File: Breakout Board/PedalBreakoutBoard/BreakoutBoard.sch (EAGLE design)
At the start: 15 parts, among them U1 ES_DAISY_SEED_REV4

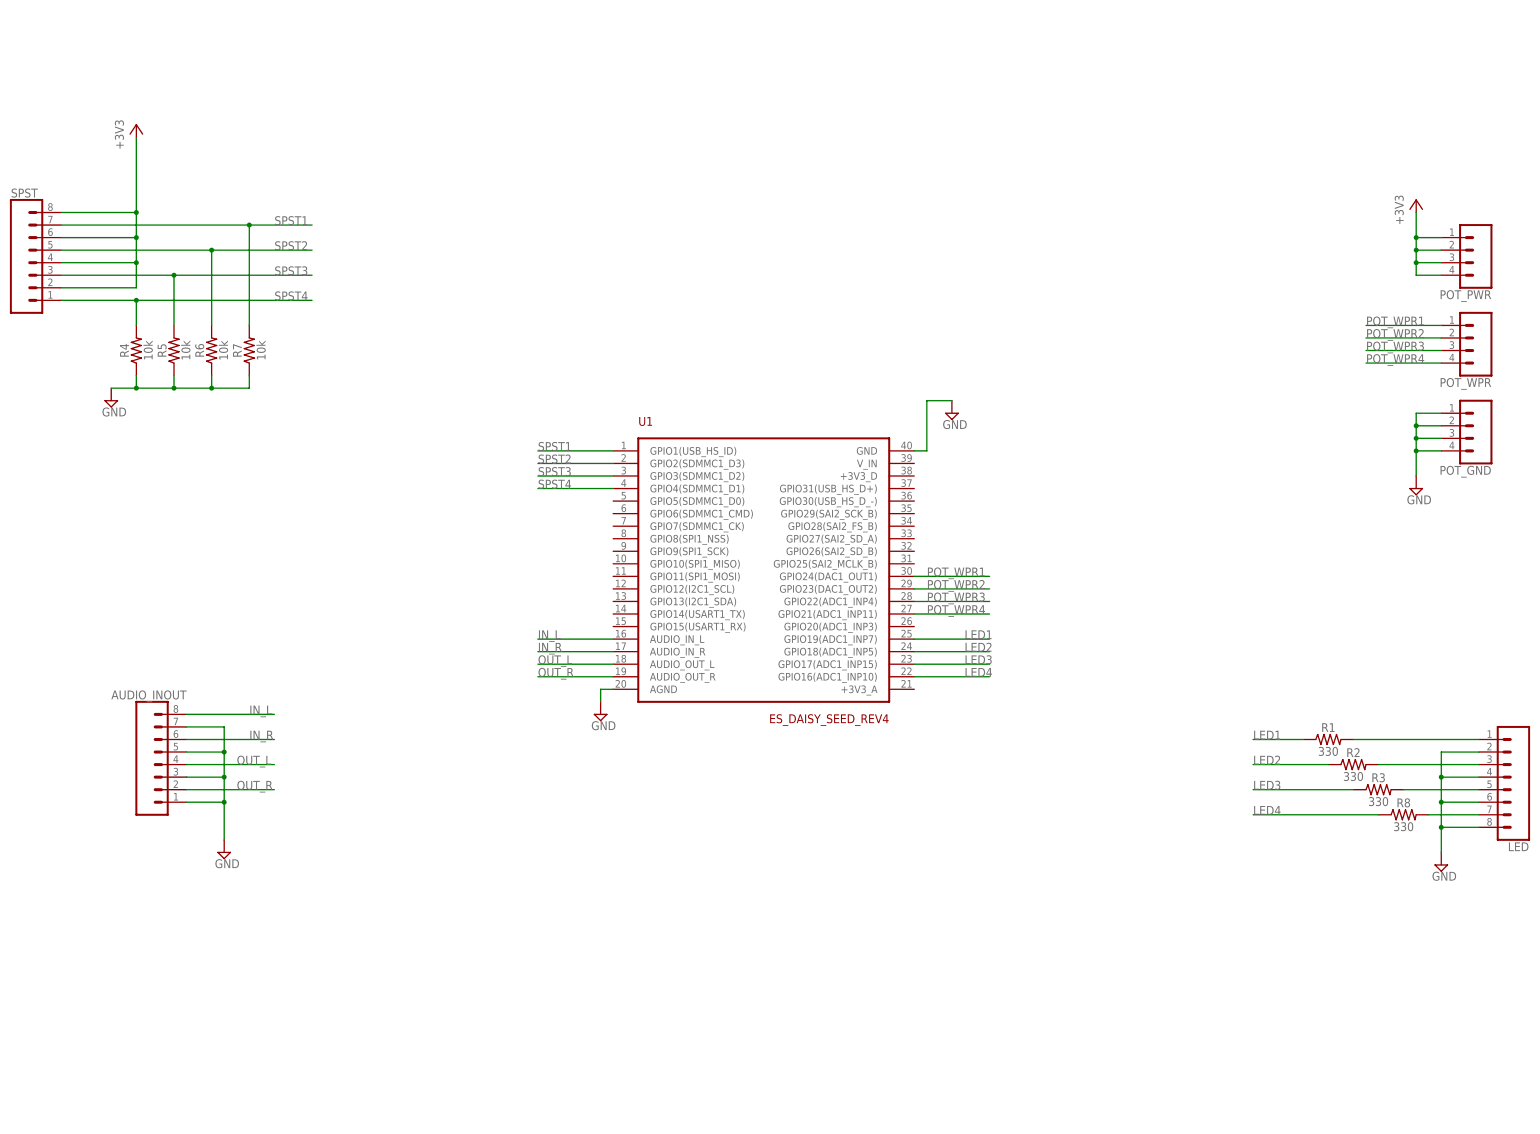
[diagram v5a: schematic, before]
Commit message: DP-16 - Add SPDT section
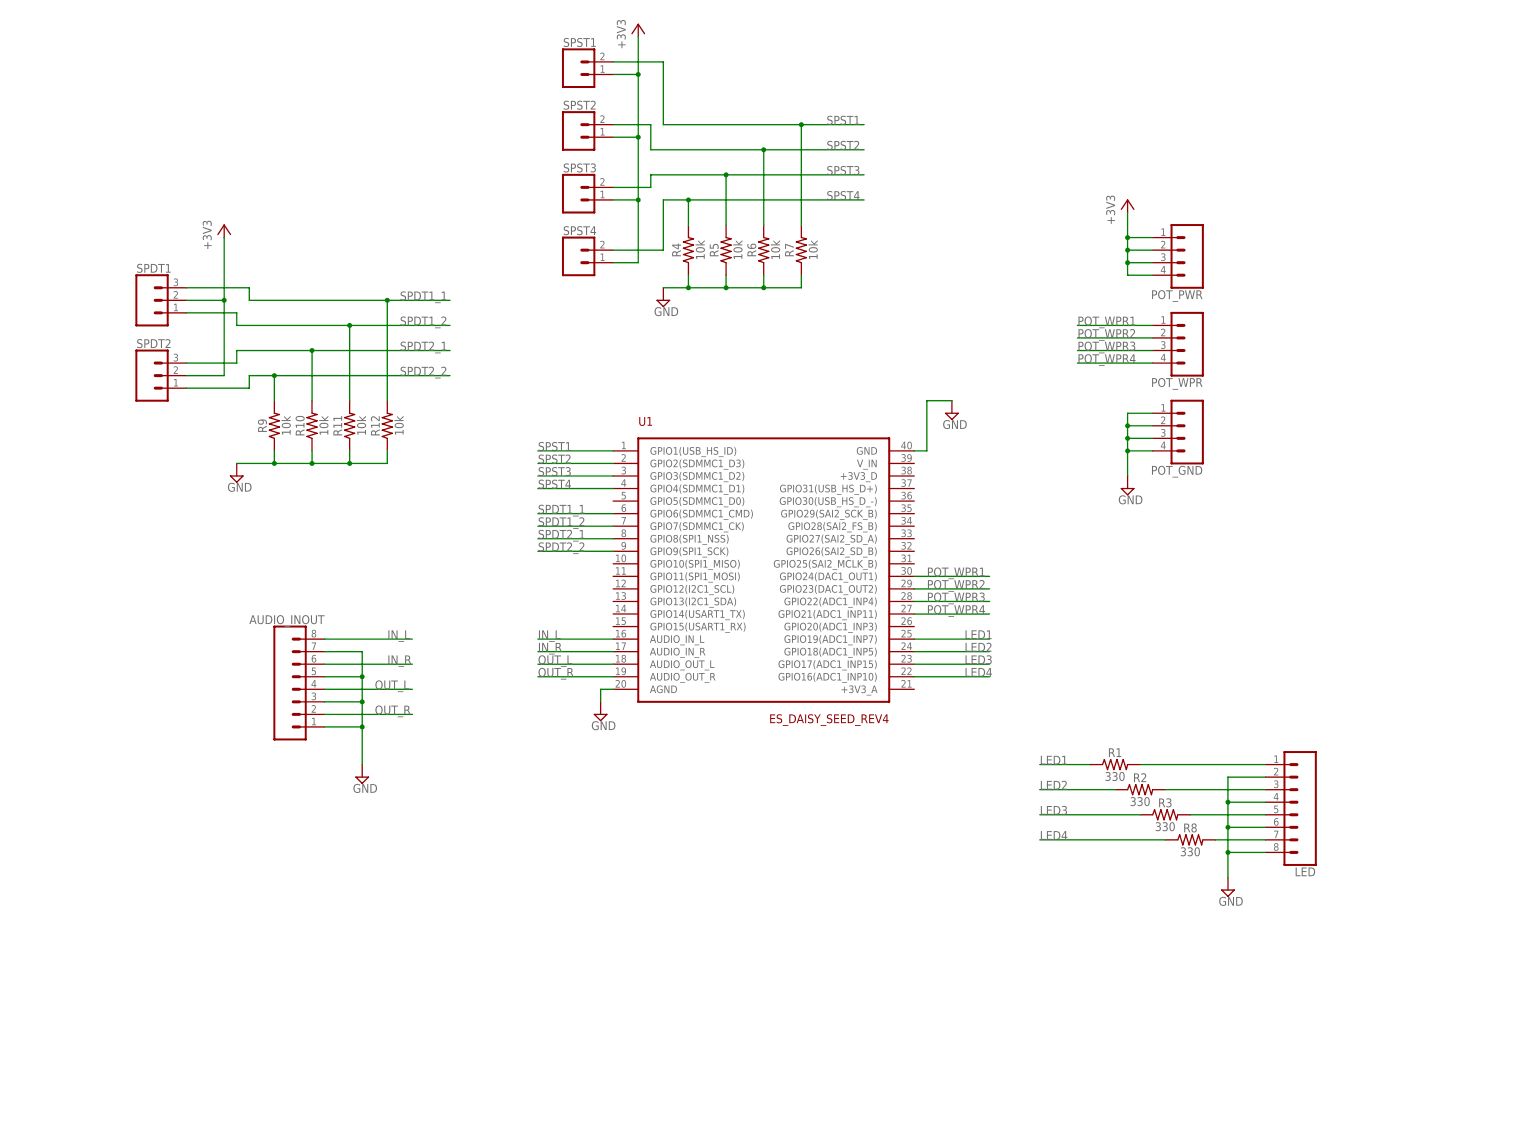
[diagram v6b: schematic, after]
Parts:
- removed SPST: (no value), SparkFun-Connectors:CONN_08"
- added R10, R11, R12, R9: 10k, SparkFun-Resistors:10KOHM-HORIZ-1/4W-5%
- added SPDT1, SPDT2: (no value), SparkFun-Connectors:CONN_03
- added SPST1, SPST2, SPST3, SPST4: (no value), SparkFun-Connectors:CONN_02
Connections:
- new net SPDT1_1: R12.2, SPDT1.3, U1.GPIO6(SDMMC1_CMD)
- new net SPDT1_2: R11.2, SPDT1.1, U1.GPIO7(SDMMC1_CK)
- new net SPDT2_1: R10.2, SPDT2.3, U1.GPIO8(SPI1_NSS)
- new net SPDT2_2: R9.2, SPDT2.1, U1.GPIO9(SPI1_SCK)
- net +3V3: now also SPDT1.2, SPDT2.2, SPST1.1, SPST2.1, SPST3.1, SPST4.1; no longer SPST.2, SPST.4, SPST.6, SPST.8
- net GND: now also R10.1, R11.1, R12.1, R9.1
- net SPST1: now also SPST1.2; no longer SPST.7
- net SPST2: now also SPST2.2; no longer SPST.5
- net SPST3: now also SPST3.2; no longer SPST.3
- net SPST4: now also SPST4.2; no longer SPST.1
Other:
- moved on the sheet: AUDIO_INOUT, LED, POT_GND, POT_PWR, POT_WPR, R1, R2, R3, R4, R5, R6, R7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

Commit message: DP-16 - Reorder groups for consistency
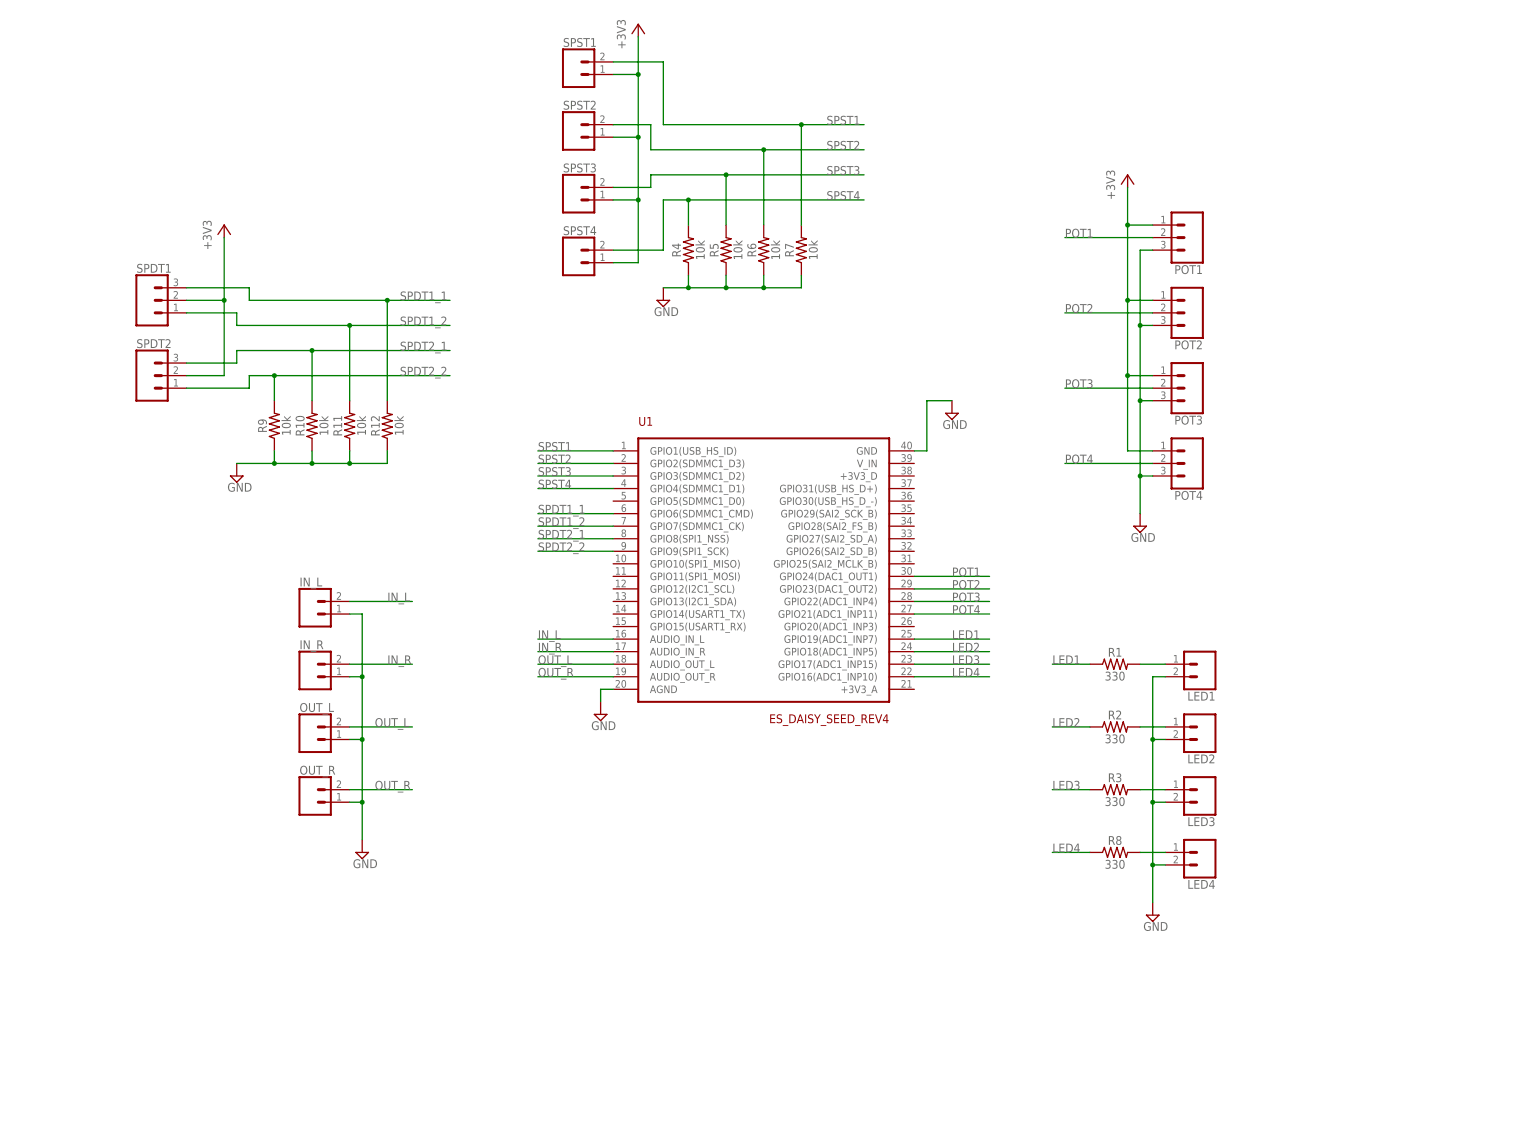
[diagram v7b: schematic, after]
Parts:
- removed AUDIO_INOUT, LED: (no value), SparkFun-Connectors:CONN_08"
- removed POT_GND, POT_PWR, POT_WPR: (no value), SparkFun-Connectors:CONN_04
- added IN_L, IN_R, LED1, LED2, LED3, LED4, OUT_L, OUT_R: (no value), SparkFun-Connectors:CONN_02
- added POT1, POT2, POT3, POT4: (no value), SparkFun-Connectors:CONN_03
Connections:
- removed net POT_WPR1: POT_WPR.1, U1.GPIO24(DAC1_OUT1)
- removed net POT_WPR2: POT_WPR.2, U1.GPIO23(DAC1_OUT2)
- removed net POT_WPR3: POT_WPR.3, U1.GPIO22(ADC1_INP4)
- removed net POT_WPR4: POT_WPR.4, U1.GPIO21(ADC1_INP11)
- new net POT1: POT1.2, U1.GPIO24(DAC1_OUT1)
- new net POT2: POT2.2, U1.GPIO23(DAC1_OUT2)
- new net POT3: POT3.2, U1.GPIO22(ADC1_INP4)
- new net POT4: POT4.2, U1.GPIO21(ADC1_INP11)
- net +3V3: now also POT1.1, POT2.1, POT3.1, POT4.1; no longer POT_PWR.1, POT_PWR.2, POT_PWR.3, POT_PWR.4
- net GND: now also IN_L.1, IN_R.1, LED1.2, LED2.2, LED3.2, LED4.2, OUT_L.1, OUT_R.1, POT1.3, POT2.3, POT3.3, POT4.3; no longer AUDIO_INOUT.1, AUDIO_INOUT.3, AUDIO_INOUT.5, AUDIO_INOUT.7, LED.2, LED.4, LED.6, LED.8, POT_GND.1, POT_GND.2, POT_GND.3, POT_GND.4
- net IN_L: now also IN_L.2; no longer AUDIO_INOUT.8
- net IN_R: now also IN_R.2; no longer AUDIO_INOUT.6
- net N$5: now also LED1.1; no longer LED.1
- net N$6: now also LED2.1; no longer LED.3
- net N$7: now also LED3.1; no longer LED.5
- net N$8: now also LED4.1; no longer LED.7
- net OUT_L: now also OUT_L.2; no longer AUDIO_INOUT.4
- net OUT_R: now also OUT_R.2; no longer AUDIO_INOUT.2
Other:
- moved on the sheet: R1, R2, R3, R8

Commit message: DP-16 - Add selector section
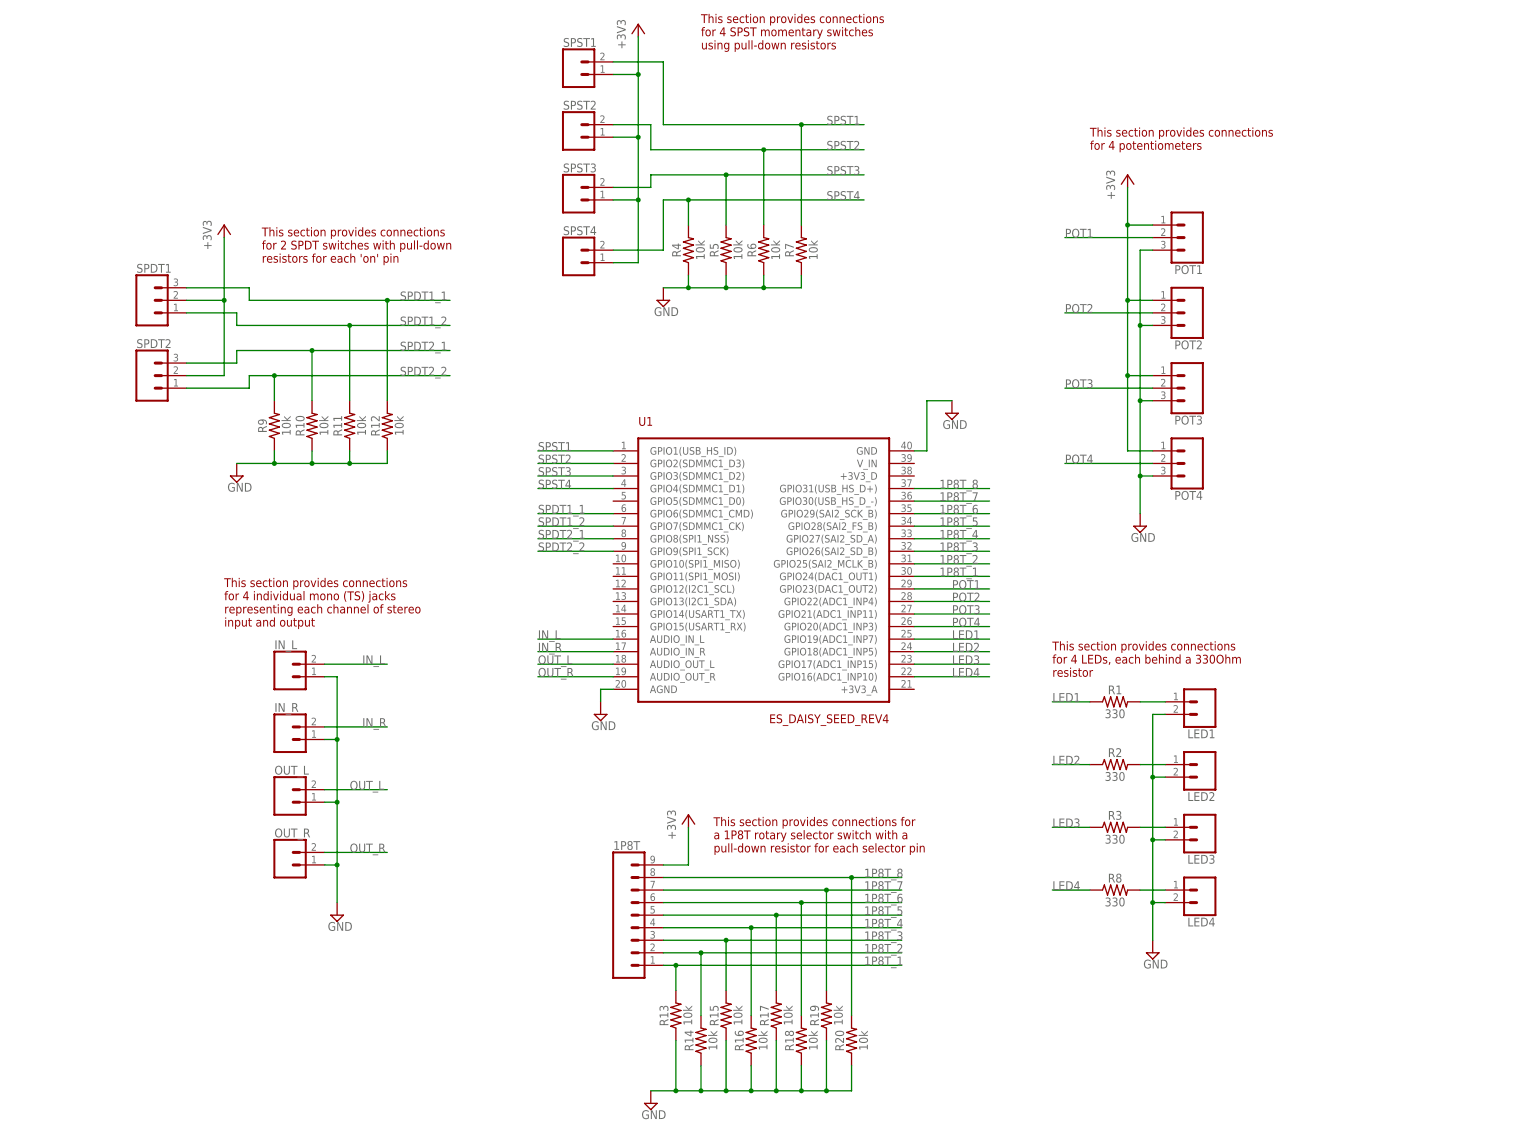
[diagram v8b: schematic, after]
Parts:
- added 1P8T: (no value), SparkFun-Connectors:CONN_09
- added R13, R14, R15, R16, R17, R18, R19, R20: 10k, SparkFun-Resistors:10KOHM-HORIZ-1/4W-5%
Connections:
- new net 1P8T_1: 1P8T.1, R13.2, U1.GPIO24(DAC1_OUT1)
- new net 1P8T_2: 1P8T.2, R14.2, U1.GPIO25(SAI2_MCLK_B)
- new net 1P8T_3: 1P8T.3, R15.2, U1.GPIO26(SAI2_SD_B)
- new net 1P8T_4: 1P8T.4, R16.2, U1.GPIO27(SAI2_SD_A)
- new net 1P8T_5: 1P8T.5, R17.2, U1.GPIO28(SAI2_FS_B)
- new net 1P8T_6: 1P8T.6, R18.2, U1.GPIO29(SAI2_SCK_B)
- new net 1P8T_7: 1P8T.7, R19.2, U1.GPIO30(USB_HS_D_-)
- new net 1P8T_8: 1P8T.8, R20.2, U1.GPIO31(USB_HS_D+)
- net +3V3: now also 1P8T.9
- net GND: now also R13.1, R14.1, R15.1, R16.1, R17.1, R18.1, R19.1, R20.1
- net POT1: now also U1.GPIO23(DAC1_OUT2); no longer U1.GPIO24(DAC1_OUT1)
- net POT2: now also U1.GPIO22(ADC1_INP4); no longer U1.GPIO23(DAC1_OUT2)
- net POT3: now also U1.GPIO21(ADC1_INP11); no longer U1.GPIO22(ADC1_INP4)
- net POT4: now also U1.GPIO20(ADC1_INP3); no longer U1.GPIO21(ADC1_INP11)
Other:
- note added: "This section provides connections for 2 SPDT switches with pull-down resistors for each 'on' pin"
- note added: "This section provides connections for 4 LEDs, each behind a 330Ohm resistor"
- note added: "This section provides connections for 4 SPST momentary switches using pull-down resistors"
- note added: "This section provides connections for 4 individual mono (TS) jacks representing each channel of stereo input and output"
- note added: "This section provides connections for 4 potentiometers"
- note added: "This section provides connections for a 1P8T rotary selector switch with a pull-down resistor for each selector pin"
- moved on the sheet: IN_L, IN_R, LED1, LED2, LED3, LED4, OUT_L, OUT_R, R1, R2, R3, R8
